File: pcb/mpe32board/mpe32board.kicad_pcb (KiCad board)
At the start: 2 copper layers, 12 parts, among them J1 Conn_ST_STDC14, J3 Conn_01x01_Socket, J4 Conn_01x04, U10 W9812G6KH-75, U2 USBLC6-2P6, U3 AMS1117-3.3, U4 TCA9548ARGER, U5 TCA9548ARGER, U6 TCA9548ARGER, U7 TCA9548ARGER, U8 TCA9548ARGER, U9 STM32H743IITx

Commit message: layout stuff
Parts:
- added C1: 4.7μF, Capacitor_SMD:C_0603_1608Metric, F.Cu at (104.7, 146.2)
- added C10: 100nF, Capacitor_SMD:C_0603_1608Metric, F.Cu at (100.4, 115.2)
- added C11: 100nF, Capacitor_SMD:C_0603_1608Metric, F.Cu at (94.8, 115.1)
- added C12: 100nF, Capacitor_SMD:C_0603_1608Metric, F.Cu at (87.8, 121.0)
- added C13: 100nF, Capacitor_SMD:C_0603_1608Metric, F.Cu at (118.6, 130.5)
- added C14: 100nF, Capacitor_SMD:C_0603_1608Metric, F.Cu at (87.7, 131.8)
- added C15: 2.2μF, Capacitor_SMD:C_0603_1608Metric, F.Cu at (96.3, 115.1)
- added C16: 2.2μF, Capacitor_SMD:C_0603_1608Metric, F.Cu at (87.6, 137.9)
- added C17: 10μF, Capacitor_SMD:C_0603_1608Metric, F.Cu at (125.8, 101.3)
- added C18: 0.1μF, Capacitor_SMD:C_0603_1608Metric, F.Cu at (125.8, 102.9)
- added C19: 10μF, Capacitor_SMD:C_0603_1608Metric, F.Cu at (125.8, 104.5)
- added C2: 100nF, Capacitor_SMD:C_0603_1608Metric, F.Cu at (105.8, 115.2)
- added C20: 0.1μF, Capacitor_SMD:C_0603_1608Metric, F.Cu at (125.8, 106.1)
- added C21: 1μF, Capacitor_SMD:C_0603_1608Metric, F.Cu at (87.7, 133.3)
- added C22: 100nF, Capacitor_SMD:C_0603_1608Metric, F.Cu at (118.6, 134.5)
- added C23: 100nF, Capacitor_SMD:C_0603_1608Metric, F.Cu at (118.6, 139.1)
- added C24: 100nF, Capacitor_SMD:C_0603_1608Metric, F.Cu at (112.0, 146.2)
- added C25: 100nF, Capacitor_SMD:C_0603_1608Metric, F.Cu at (118.5, 122.4)
- added C26: 10μF, Capacitor_SMD:C_0603_1608Metric, F.Cu at (125.4, 112.4)
- added C27: 0.1μF, Capacitor_SMD:C_0603_1608Metric, F.Cu at (126.9, 112.4)
- added C28: 1μF, Capacitor_SMD:C_0603_1608Metric, F.Cu at (123.9, 112.4)
- added C29: 0.1μF, Capacitor_SMD:C_0603_1608Metric, F.Cu at (123.1, 116.1)
- added C3: 100nF, Capacitor_SMD:C_0603_1608Metric, F.Cu at (111.9, 115.3)
- added C30: 10μF, Capacitor_SMD:C_0603_1608Metric, F.Cu at (123.1, 114.6)
- added C31: 0.1μF, Capacitor_SMD:C_0603_1608Metric, F.Cu at (123.1, 117.5)
- added C32: 10μF, Capacitor_SMD:C_0603_1608Metric, F.Cu at (123.1, 119.0)
- added C33: 47μF, Capacitor_SMD:C_0603_1608Metric, F.Cu at (129.8, 112.4)
- added C34: 47μF, Capacitor_SMD:C_0603_1608Metric, F.Cu at (128.4, 112.4)
- added C4: 100nF, Capacitor_SMD:C_0603_1608Metric, F.Cu at (87.7, 126.9)
- added C5: 100nF, Capacitor_SMD:C_0603_1608Metric, F.Cu at (87.6, 139.3)
- added C6: 100nF, Capacitor_SMD:C_0603_1608Metric, F.Cu at (93.9, 146.2)
- added C7: 100nF, Capacitor_SMD:C_0603_1608Metric, F.Cu at (100.5, 146.2)
- added C8: 100nF, Capacitor_SMD:C_0603_1608Metric, F.Cu at (106.2, 146.2)
- added C9: 100nF, Capacitor_SMD:C_0603_1608Metric, F.Cu at (118.6, 124.0)
- added D1: WS2812B, LED_SMD:LED_WS2812B_PLCC4_5.0x5.0mm_P3.2mm, F.Cu at (70.0, 172.0)
- added D2: WS2812B, LED_SMD:LED_WS2812B_PLCC4_5.0x5.0mm_P3.2mm, F.Cu at (79.8, 172.0)
- added D3: WS2812B, LED_SMD:LED_WS2812B_PLCC4_5.0x5.0mm_P3.2mm, F.Cu at (89.6, 172.0)
- added D4: WS2812B, LED_SMD:LED_WS2812B_PLCC4_5.0x5.0mm_P3.2mm, F.Cu at (99.5, 172.0)
- added D5: WS2812B, LED_SMD:LED_WS2812B_PLCC4_5.0x5.0mm_P3.2mm, F.Cu at (109.3, 172.0)
- added D6: WS2812B, LED_SMD:LED_WS2812B_PLCC4_5.0x5.0mm_P3.2mm, F.Cu at (119.1, 172.0)
- added D7: WS2812B, LED_SMD:LED_WS2812B_PLCC4_5.0x5.0mm_P3.2mm, F.Cu at (128.9, 172.0)
- added D8: WS2812B, LED_SMD:LED_WS2812B_PLCC4_5.0x5.0mm_P3.2mm, F.Cu at (138.7, 172.0)
- added J10: Conn_01x04, Connector_JST:JST_SH_BM04B-SRSS-TB_1x04-1MP_P1.00mm_Vertical, F.Cu at (150.6, 140.4)
- added J11: Conn_01x04, Connector_JST:JST_SH_BM04B-SRSS-TB_1x04-1MP_P1.00mm_Vertical, F.Cu at (150.6, 145.7)
- added J12: Conn_01x04, Connector_JST:JST_SH_BM04B-SRSS-TB_1x04-1MP_P1.00mm_Vertical, F.Cu at (150.6, 151.0)
- added J13: Conn_01x04, Connector_JST:JST_SH_BM04B-SRSS-TB_1x04-1MP_P1.00mm_Vertical, F.Cu at (150.6, 156.3)
- added J14: Conn_01x04, Connector_JST:JST_SH_BM04B-SRSS-TB_1x04-1MP_P1.00mm_Vertical, F.Cu at (150.6, 161.6)
- added J15: Conn_01x04, Connector_JST:JST_SH_BM04B-SRSS-TB_1x04-1MP_P1.00mm_Vertical, F.Cu at (150.6, 166.8)
- added J16: Conn_01x04, Connector_JST:JST_SH_BM04B-SRSS-TB_1x04-1MP_P1.00mm_Vertical, F.Cu at (159.1, 108.7)
- added J17: Conn_01x04, Connector_JST:JST_SH_BM04B-SRSS-TB_1x04-1MP_P1.00mm_Vertical, F.Cu at (159.1, 114.0)
- added J18: Conn_01x04, Connector_JST:JST_SH_BM04B-SRSS-TB_1x04-1MP_P1.00mm_Vertical, F.Cu at (159.1, 119.2)
- added J19: Conn_01x04, Connector_JST:JST_SH_BM04B-SRSS-TB_1x04-1MP_P1.00mm_Vertical, F.Cu at (159.1, 124.5)
- added J2: USB_C_Receptacle_USB2.0_16P, Connector_USB:USB_C_Receptacle_GCT_USB4105-xx-A_16P_TopMnt_Horizontal, F.Cu at (121.6, 92.1)
- added J20: Conn_01x04, Connector_JST:JST_SH_BM04B-SRSS-TB_1x04-1MP_P1.00mm_Vertical, F.Cu at (159.1, 129.8)
- added J21: Conn_01x04, Connector_JST:JST_SH_BM04B-SRSS-TB_1x04-1MP_P1.00mm_Vertical, F.Cu at (159.1, 135.1)
- added J22: Conn_01x04, Connector_JST:JST_SH_BM04B-SRSS-TB_1x04-1MP_P1.00mm_Vertical, F.Cu at (159.1, 140.4)
- added J23: Conn_01x04, Connector_JST:JST_SH_BM04B-SRSS-TB_1x04-1MP_P1.00mm_Vertical, F.Cu at (159.1, 145.7)
- added J24: Conn_01x04, Connector_JST:JST_SH_BM04B-SRSS-TB_1x04-1MP_P1.00mm_Vertical, F.Cu at (159.1, 151.0)
- added J25: Conn_01x04, Connector_JST:JST_SH_BM04B-SRSS-TB_1x04-1MP_P1.00mm_Vertical, F.Cu at (159.1, 156.3)
- added J26: Conn_01x04, Connector_JST:JST_SH_BM04B-SRSS-TB_1x04-1MP_P1.00mm_Vertical, F.Cu at (159.1, 161.6)
- added J27: Conn_01x04, Connector_JST:JST_SH_BM04B-SRSS-TB_1x04-1MP_P1.00mm_Vertical, F.Cu at (159.1, 166.8)
- added J28: Conn_01x04, Connector_JST:JST_SH_BM04B-SRSS-TB_1x04-1MP_P1.00mm_Vertical, F.Cu at (167.3, 108.7)
- added J29: Conn_01x04, Connector_JST:JST_SH_BM04B-SRSS-TB_1x04-1MP_P1.00mm_Vertical, F.Cu at (167.3, 114.0)
- added J30: Conn_01x04, Connector_JST:JST_SH_BM04B-SRSS-TB_1x04-1MP_P1.00mm_Vertical, F.Cu at (167.3, 119.2)
- added J31: Conn_01x04, Connector_JST:JST_SH_BM04B-SRSS-TB_1x04-1MP_P1.00mm_Vertical, F.Cu at (167.3, 124.5)
- added J32: Conn_01x04, Connector_JST:JST_SH_BM04B-SRSS-TB_1x04-1MP_P1.00mm_Vertical, F.Cu at (167.3, 129.8)
- added J33: Conn_01x04, Connector_JST:JST_SH_BM04B-SRSS-TB_1x04-1MP_P1.00mm_Vertical, F.Cu at (167.3, 135.1)
- added J34: Conn_01x04, Connector_JST:JST_SH_BM04B-SRSS-TB_1x04-1MP_P1.00mm_Vertical, F.Cu at (167.3, 140.4)
- added J35: Conn_01x04, Connector_JST:JST_SH_BM04B-SRSS-TB_1x04-1MP_P1.00mm_Vertical, F.Cu at (167.3, 145.7)
- added J36: Conn_01x04, Connector_JST:JST_SH_BM04B-SRSS-TB_1x04-1MP_P1.00mm_Vertical, F.Cu at (167.3, 151.0)
- added J37: Conn_01x04, Connector_JST:JST_SH_BM04B-SRSS-TB_1x04-1MP_P1.00mm_Vertical, F.Cu at (167.3, 156.3)
- added J38: Conn_01x04, Connector_JST:JST_SH_BM04B-SRSS-TB_1x04-1MP_P1.00mm_Vertical, F.Cu at (167.3, 161.6)
- added J39: Conn_01x04, Connector_JST:JST_SH_BM04B-SRSS-TB_1x04-1MP_P1.00mm_Vertical, F.Cu at (167.3, 166.8)
- added J40: Conn_01x04, Connector_JST:JST_SH_BM04B-SRSS-TB_1x04-1MP_P1.00mm_Vertical, F.Cu at (147.2, 100.0)
- added J41: Conn_01x04, Connector_JST:JST_SH_BM04B-SRSS-TB_1x04-1MP_P1.00mm_Vertical, F.Cu at (152.4, 100.0)
- added J42: Conn_01x04, Connector_JST:JST_SH_BM04B-SRSS-TB_1x04-1MP_P1.00mm_Vertical, F.Cu at (157.6, 100.0)
- added J43: Conn_01x04, Connector_JST:JST_SH_BM04B-SRSS-TB_1x04-1MP_P1.00mm_Vertical, F.Cu at (162.8, 100.0)
- added J44: Micro_SD_Card, Connector_Card:microSD_HC_Molex_47219-2001, F.Cu at (107.2, 97.1)
- added J45: Conn_01x04_Socket, Connector_PinHeader_2.54mm:PinHeader_1x04_P2.54mm_Vertical, F.Cu at (69.1, 130.4)
- added J46: Conn_02x10_Counter_Clockwise, Connector_PinHeader_2.54mm:PinHeader_2x10_P2.54mm_Vertical, F.Cu at (145.3, 94.0)
- added J47: AudioJack3_Ground, Connector_Audio:Jack_3.5mm_CUI_SJ-3524-SMT_Horizontal, F.Cu at (133.1, 95.1)
- added J5: Conn_01x04, Connector_JST:JST_SH_BM04B-SRSS-TB_1x04-1MP_P1.00mm_Vertical, F.Cu at (150.6, 114.0)
- added J6: Conn_01x04, Connector_JST:JST_SH_BM04B-SRSS-TB_1x04-1MP_P1.00mm_Vertical, F.Cu at (150.6, 119.2)
- added J7: Conn_01x04, Connector_JST:JST_SH_BM04B-SRSS-TB_1x04-1MP_P1.00mm_Vertical, F.Cu at (150.6, 124.5)
- added J8: Conn_01x04, Connector_JST:JST_SH_BM04B-SRSS-TB_1x04-1MP_P1.00mm_Vertical, F.Cu at (150.6, 129.8)
- added J9: Conn_01x04, Connector_JST:JST_SH_BM04B-SRSS-TB_1x04-1MP_P1.00mm_Vertical, F.Cu at (150.6, 135.1)
- added R1: 10kΩ, Resistor_SMD:R_0603_1608Metric, F.Cu at (87.7, 96.1)
- added R10: 2.2kΩ, Resistor_SMD:R_0603_1608Metric, F.Cu at (139.2, 119.5)
- added R11: 2.2kΩ, Resistor_SMD:R_0603_1608Metric, F.Cu at (141.4, 115.7)
- added R12: 2.2kΩ, Resistor_SMD:R_0603_1608Metric, F.Cu at (141.4, 117.2)
- added R13: 2.2kΩ, Resistor_SMD:R_0603_1608Metric, F.Cu at (141.4, 112.7)
- added R14: 2.2kΩ, Resistor_SMD:R_0603_1608Metric, F.Cu at (141.4, 114.2)
- added R15: 2.2kΩ, Resistor_SMD:R_0603_1608Metric, F.Cu at (139.2, 110.5)
- added R16: 2.2kΩ, Resistor_SMD:R_0603_1608Metric, F.Cu at (140.7, 110.5)
- added R17: 2.2kΩ, Resistor_SMD:R_0603_1608Metric, F.Cu at (136.2, 110.5)
- added R18: 2.2kΩ, Resistor_SMD:R_0603_1608Metric, F.Cu at (137.7, 110.5)
- added R19: 2.2kΩ, Resistor_SMD:R_0603_1608Metric, F.Cu at (133.3, 110.5)
- added R2: 10kΩ, Resistor_SMD:R_0603_1608Metric, F.Cu at (87.7, 98.6)
- added R20: 2.2kΩ, Resistor_SMD:R_0603_1608Metric, F.Cu at (134.7, 110.5)
- added R21: 10kΩ, Resistor_SMD:R_0603_1608Metric, F.Cu at (107.6, 146.2)
- added R22: 10kΩ, Resistor_SMD:R_0603_1608Metric, F.Cu at (109.1, 146.2)
- added R23: 10kΩ, Resistor_SMD:R_0603_1608Metric, F.Cu at (114.9, 115.3)
- added R24: 10kΩ, Resistor_SMD:R_0603_1608Metric, F.Cu at (113.4, 115.3)
- added R25: 2.2kΩ, Resistor_SMD:R_0603_1608Metric, F.Cu at (123.7, 147.9)
- added R26: 2.2kΩ, Resistor_SMD:R_0603_1608Metric, F.Cu at (122.2, 147.9)
- added R27: 2.2kΩ, Resistor_SMD:R_0603_1608Metric, F.Cu at (126.7, 147.9)
- added R28: 2.2kΩ, Resistor_SMD:R_0603_1608Metric, F.Cu at (125.2, 147.9)
- added R29: 2.2kΩ, Resistor_SMD:R_0603_1608Metric, F.Cu at (129.6, 147.9)
- added R3: 5.1kΩ, Resistor_SMD:R_0603_1608Metric, F.Cu at (123.7, 97.6)
- added R30: 2.2kΩ, Resistor_SMD:R_0603_1608Metric, F.Cu at (128.2, 147.9)
- added R31: 2.2kΩ, Resistor_SMD:R_0603_1608Metric, F.Cu at (130.3, 144.2)
- added R32: 2.2kΩ, Resistor_SMD:R_0603_1608Metric, F.Cu at (130.3, 145.7)
- added R33: 2.2kΩ, Resistor_SMD:R_0603_1608Metric, F.Cu at (130.3, 141.2)
- added R34: 2.2kΩ, Resistor_SMD:R_0603_1608Metric, F.Cu at (130.3, 142.7)
- added R35: 2.2kΩ, Resistor_SMD:R_0603_1608Metric, F.Cu at (128.1, 139.0)
- added R36: 2.2kΩ, Resistor_SMD:R_0603_1608Metric, F.Cu at (129.6, 139.0)
- added R37: 2.2kΩ, Resistor_SMD:R_0603_1608Metric, F.Cu at (125.2, 139.0)
- added R38: 2.2kΩ, Resistor_SMD:R_0603_1608Metric, F.Cu at (126.7, 139.0)
- added R39: 2.2kΩ, Resistor_SMD:R_0603_1608Metric, F.Cu at (122.3, 139.0)
- added R4: 5.1kΩ, Resistor_SMD:R_0603_1608Metric, F.Cu at (119.4, 98.4)
- added R40: 2.2kΩ, Resistor_SMD:R_0603_1608Metric, F.Cu at (123.7, 139.0)
- added R41: 1kΩ, Resistor_SMD:R_0603_1608Metric, F.Cu at (92.4, 115.1)
- added R42: 1kΩ, Resistor_SMD:R_0603_1608Metric, F.Cu at (87.8, 119.5)
- added R43: 2.2kΩ, Resistor_SMD:R_0603_1608Metric, F.Cu at (123.7, 135.3)
- added R44: 2.2kΩ, Resistor_SMD:R_0603_1608Metric, F.Cu at (122.2, 135.3)
- added R45: 2.2kΩ, Resistor_SMD:R_0603_1608Metric, F.Cu at (126.7, 135.3)
- added R46: 2.2kΩ, Resistor_SMD:R_0603_1608Metric, F.Cu at (125.2, 135.3)
- added R47: 2.2kΩ, Resistor_SMD:R_0603_1608Metric, F.Cu at (129.6, 135.3)
- added R48: 2.2kΩ, Resistor_SMD:R_0603_1608Metric, F.Cu at (128.1, 135.3)
- added R49: 2.2kΩ, Resistor_SMD:R_0603_1608Metric, F.Cu at (130.3, 131.6)
- added R5: 2.2kΩ, Resistor_SMD:R_0603_1608Metric, F.Cu at (134.7, 119.5)
- added R50: 2.2kΩ, Resistor_SMD:R_0603_1608Metric, F.Cu at (130.3, 133.1)
- added R51: 2.2kΩ, Resistor_SMD:R_0603_1608Metric, F.Cu at (130.3, 128.6)
- added R52: 2.2kΩ, Resistor_SMD:R_0603_1608Metric, F.Cu at (130.3, 130.1)
- added R53: 2.2kΩ, Resistor_SMD:R_0603_1608Metric, F.Cu at (128.1, 126.4)
- added R54: 2.2kΩ, Resistor_SMD:R_0603_1608Metric, F.Cu at (129.6, 126.4)
- added R55: 2.2kΩ, Resistor_SMD:R_0603_1608Metric, F.Cu at (125.1, 126.4)
- added R56: 2.2kΩ, Resistor_SMD:R_0603_1608Metric, F.Cu at (126.6, 126.4)
- added R57: 2.2kΩ, Resistor_SMD:R_0603_1608Metric, F.Cu at (122.2, 126.4)
- added R58: 2.2kΩ, Resistor_SMD:R_0603_1608Metric, F.Cu at (123.7, 126.4)
- added R59: 10kΩ, Resistor_SMD:R_0603_1608Metric, F.Cu at (78.8, 150.7)
- added R6: 2.2kΩ, Resistor_SMD:R_0603_1608Metric, F.Cu at (133.2, 119.5)
- added R60: 10kΩ, Resistor_SMD:R_0603_1608Metric, F.Cu at (98.0, 150.7)
- added R61: 2.2kΩ, Resistor_SMD:R_0603_1608Metric, F.Cu at (134.9, 132.9)
- added R62: 2.2kΩ, Resistor_SMD:R_0603_1608Metric, F.Cu at (133.4, 132.9)
- added R63: 2.2kΩ, Resistor_SMD:R_0603_1608Metric, F.Cu at (137.8, 132.9)
- added R64: 2.2kΩ, Resistor_SMD:R_0603_1608Metric, F.Cu at (136.3, 132.9)
- added R65: 2.2kΩ, Resistor_SMD:R_0603_1608Metric, F.Cu at (140.8, 132.9)
- added R66: 2.2kΩ, Resistor_SMD:R_0603_1608Metric, F.Cu at (139.3, 132.9)
- added R67: 2.2kΩ, Resistor_SMD:R_0603_1608Metric, F.Cu at (141.5, 129.2)
- added R68: 2.2kΩ, Resistor_SMD:R_0603_1608Metric, F.Cu at (141.5, 130.6)
- added R69: 2.2kΩ, Resistor_SMD:R_0603_1608Metric, F.Cu at (141.5, 126.2)
- added R7: 2.2kΩ, Resistor_SMD:R_0603_1608Metric, F.Cu at (137.7, 119.5)
- added R70: 2.2kΩ, Resistor_SMD:R_0603_1608Metric, F.Cu at (141.5, 127.7)
- added R71: 2.2kΩ, Resistor_SMD:R_0603_1608Metric, F.Cu at (139.3, 123.9)
- added R72: 2.2kΩ, Resistor_SMD:R_0603_1608Metric, F.Cu at (140.8, 123.9)
- added R73: 2.2kΩ, Resistor_SMD:R_0603_1608Metric, F.Cu at (136.3, 123.9)
- added R74: 2.2kΩ, Resistor_SMD:R_0603_1608Metric, F.Cu at (137.8, 123.9)
- added R75: 2.2kΩ, Resistor_SMD:R_0603_1608Metric, F.Cu at (133.3, 123.9)
- added R76: 2.2kΩ, Resistor_SMD:R_0603_1608Metric, F.Cu at (134.8, 123.9)
- added R77: 10kΩ, Resistor_SMD:R_0603_1608Metric, F.Cu at (117.1, 150.7)
- added R78: 10kΩ, Resistor_SMD:R_0603_1608Metric, F.Cu at (136.2, 150.7)
- added R79: 2.2kΩ, Resistor_SMD:R_0603_1608Metric, F.Cu at (134.9, 147.3)
- added R8: 2.2kΩ, Resistor_SMD:R_0603_1608Metric, F.Cu at (136.2, 119.5)
- added R80: 2.2kΩ, Resistor_SMD:R_0603_1608Metric, F.Cu at (133.4, 147.3)
- added R81: 2.2kΩ, Resistor_SMD:R_0603_1608Metric, F.Cu at (137.8, 147.3)
- added R82: 2.2kΩ, Resistor_SMD:R_0603_1608Metric, F.Cu at (136.4, 147.3)
- added R83: 2.2kΩ, Resistor_SMD:R_0603_1608Metric, F.Cu at (140.8, 147.3)
- added R84: 2.2kΩ, Resistor_SMD:R_0603_1608Metric, F.Cu at (139.3, 147.3)
- added R85: 2.2kΩ, Resistor_SMD:R_0603_1608Metric, F.Cu at (141.5, 143.6)
- added R86: 2.2kΩ, Resistor_SMD:R_0603_1608Metric, F.Cu at (141.5, 145.1)
- added R87: 2.2kΩ, Resistor_SMD:R_0603_1608Metric, F.Cu at (141.5, 140.7)
- added R88: 2.2kΩ, Resistor_SMD:R_0603_1608Metric, F.Cu at (141.5, 142.2)
- added R89: 2.2kΩ, Resistor_SMD:R_0603_1608Metric, F.Cu at (139.3, 138.4)
- added R9: 2.2kΩ, Resistor_SMD:R_0603_1608Metric, F.Cu at (140.7, 119.5)
- added R90: 2.2kΩ, Resistor_SMD:R_0603_1608Metric, F.Cu at (140.8, 138.4)
- added R91: 2.2kΩ, Resistor_SMD:R_0603_1608Metric, F.Cu at (136.3, 138.4)
- added R92: 2.2kΩ, Resistor_SMD:R_0603_1608Metric, F.Cu at (137.8, 138.4)
- added R93: 2.2kΩ, Resistor_SMD:R_0603_1608Metric, F.Cu at (133.4, 138.4)
- added R94: 2.2kΩ, Resistor_SMD:R_0603_1608Metric, F.Cu at (134.9, 138.4)
- added R95: 47kΩ, Resistor_SMD:R_0603_1608Metric, F.Cu at (104.3, 107.4)
- added R96: 47kΩ, Resistor_SMD:R_0603_1608Metric, F.Cu at (101.4, 107.3)
- added R97: 47kΩ, Resistor_SMD:R_0603_1608Metric, F.Cu at (102.8, 107.3)
- added R98: 47kΩ, Resistor_SMD:R_0603_1608Metric, F.Cu at (108.6, 107.3)
- added R99: 47kΩ, Resistor_SMD:R_0603_1608Metric, F.Cu at (110.1, 107.3)
- added SW1: SW_Push, Button_Switch_THT:SW_PUSH_6mm, F.Cu at (91.2, 90.6)
- added SW2: SW_Push, Button_Switch_THT:SW_PUSH_6mm, F.Cu at (91.2, 99.1)
- added SW3: SW_Push, Button_Switch_Keyboard:SW_Cherry_MX_1.00u_PCB, F.Cu at (78.0, 154.0)
- added SW4: SW_Push, Button_Switch_Keyboard:SW_Cherry_MX_1.00u_PCB, F.Cu at (97.1, 154.0)
- added SW5: SW_Push, Button_Switch_Keyboard:SW_Cherry_MX_1.00u_PCB, F.Cu at (116.2, 154.0)
- added SW6: SW_Push, Button_Switch_Keyboard:SW_Cherry_MX_1.00u_PCB, F.Cu at (135.3, 154.0)
- added U1: TAC5212IRGER, 1_udu_lib:VQFN24_RGE_CORNERPADS_TEX-L, F.Cu at (127.3, 116.6)
- moved U5 79.9 mm to (125.5, 143.5), turned to 90 degrees
- moved U6 65.4 mm to (125.5, 130.9), turned to 90 degrees
- moved U9 58.9 mm to (103.2, 130.8), turned to 180 degrees
- moved U8 57.5 mm to (136.7, 142.9), turned to 90 degrees
- moved U10 57.0 mm to (78.4, 130.4), turned to 180 degrees
- moved U4 55.5 mm to (136.6, 115.0), turned to 90 degrees
- moved J1 54.0 mm to (75.3, 97.7), turned to 90 degrees
- moved U7 51.2 mm to (136.7, 128.4), turned to 90 degrees
- moved J3 45.8 mm to (168.0, 98.0)
- moved U3 38.3 mm to (119.6, 105.3), turned to 180 degrees
- moved J4 22.7 mm to (150.6, 108.7)
- moved U2 14.3 mm to (122.0, 100.1)
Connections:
- net SWO renamed JTDO
- U4 pad 19: SCL_0 -> I2C2_SCL
- U4 pad 20: SDA_0 -> I2C2_SDA
- U5 pad 19: SCL_1 -> I2C2_SCL
- U5 pad 20: SDA_1 -> I2C2_SDA
- U5 pad 22: GND -> +3V3
- U6 pad 19: SCL_2 -> I2C2_SCL
- U6 pad 20: SDA_2 -> I2C2_SDA
- U6 pad 23: GND -> +3V3
- U7 pad 19: SCL_3 -> I2C2_SCL
- U7 pad 20: SDA_3 -> I2C2_SDA
- U7 pad 22: GND -> +3V3
- U7 pad 23: GND -> +3V3
- U8 pad 19: SCL_1 -> I2C2_SCL
- U8 pad 20: SDA_1 -> I2C2_SDA
- U9 pad 117: unconnected-(U9-PC8-Pad117) -> SDMMC1_D0
- U9 pad 118: SDA_3 -> SDMMC1_D1
- U9 pad 119: SCL_3 -> unconnected-(U9-PA8-Pad119)
- U9 pad 139: unconnected-(U9-PC10-Pad139) -> SDMMC1_D2
- U9 pad 140: unconnected-(U9-PC11-Pad140) -> SDMMC1_D3
- U9 pad 141: unconnected-(U9-PC12-Pad141) -> SDMMC1_CK
- U9 pad 144: unconnected-(U9-PD2-Pad144) -> SDMMC1_CMD
- U9 pad 164: SCL_0 -> I2C1_SCL
- U9 pad 165: SDA_0 -> I2C1_SDA
- U9 pad 167: SCL_1 -> unconnected-(U9-PB8-Pad167)
- U9 pad 168: SDA_1 -> unconnected-(U9-PB9-Pad168)
- U9 pad 42: unconnected-(U9-PA2-Pad42) -> NEOPIXEL_INTERNAL
- U9 pad 45: unconnected-(U9-PH4-Pad45) -> I2C2_SCL
- U9 pad 46: unconnected-(U9-PH5-Pad46) -> I2C2_SDA
- U9 pad 47: unconnected-(U9-PA3-Pad47) -> NEOPIXEL_IN
- U9 pad 50: unconnected-(U9-PA4-Pad50) -> I2S1_WS
- U9 pad 51: unconnected-(U9-PA5-Pad51) -> I2S1_CK
- U9 pad 52: unconnected-(U9-PA6-Pad52) -> I2S1_SDI
- U9 pad 53: unconnected-(U9-PA7-Pad53) -> I2S1_SDO
- U9 pad 79: SCL_2 -> TAC5212_GPIO1
- U9 pad 80: SDA_2 -> TAC5212_GPIO2
- U9 pad 88: unconnected-(U9-PH11-Pad88) -> I2C4_SCL
- U9 pad 89: unconnected-(U9-PH12-Pad89) -> I2C4_SDA
- U9 pad 92: unconnected-(U9-PB12-Pad92) -> TAC5212_GPO1
- U9 pad 93: unconnected-(U9-PB13-Pad93) -> TAC5212_GPI1
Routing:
- added copper zone on In2.Cu, net +3V3
- added copper zone on In1.Cu, net GND
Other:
- board outline added: 107 x 87 mm
- copper layers 2 -> 4

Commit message: board layout stuff
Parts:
- removed J28, J29, J30, J31, J32, J33, J34, J35, J36, J37, J38, J39, J40, J41, J42, J43: Conn_01x04, Connector_JST:JST_SH_BM04B-SRSS-TB_1x04-1MP_P1.00mm_Vertical
- removed R61, R62, R63, R64, R65, R66, R67, R68, R69, R70, R71, R72, R73, R74, R75, R76, R79, R80, R81, R82, R83, R84, R85, R86, R87, R88, R89, R90, R91, R92, R93, R94: 2.2kΩ, Resistor_SMD:R_0603_1608Metric
- removed U7, U8: TCA9548ARGER, Package_DFN_QFN:Texas_RGE0024C_VQFN-24-1EP_4x4mm_P0.5mm_EP2.1x2.1mm
- added H1: MountingHole_Pad, MountingHole:MountingHole_3.2mm_M3_DIN965_Pad, F.Cu at (72.7, 91.5)
- added H2: MountingHole_Pad, MountingHole:MountingHole_3.2mm_M3_DIN965_Pad, F.Cu at (131.9, 91.5)
- added H3: MountingHole_Pad, MountingHole:MountingHole_3.2mm_M3_DIN965_Pad, F.Cu at (131.9, 135.1)
- added H4: MountingHole_Pad, MountingHole:MountingHole_3.2mm_M3_DIN965_Pad, F.Cu at (72.7, 135.1)
- added J48: Micro_SD_Card_Det_Hirose_DM3AT, Connector_Card:microSD_HC_Hirose_DM3D-SF, F.Cu at (92.3, 87.2)
- added U11: IP4252CZ16, Package_SON:Nexperia_HUSON-16_USON-16-1EP_1.35x3.3mm_P0.4mm_EP0.4x2.8mm, F.Cu at (100.8, 85.0)
- J44: value Micro_SD_Card -> Conn_01x05; footprint Connector_Card:microSD_HC_Molex_47219-2001 -> Connector_Molex:Molex_SL_171971-0005_1x05_P2.54mm_Vertical
- moved J47 67.3 mm to (66.4, 86.0)
- moved C34 58.4 mm to (71.5, 99.6)
- moved C26 58.2 mm to (68.4, 100.4)
- moved C27 58.2 mm to (69.9, 100.4)
- moved C28 58.2 mm to (66.9, 100.4)
- moved C33 58.1 mm to (73.0, 100.4)
- moved C29 58.1 mm to (66.3, 104.1)
- moved C30 58.1 mm to (66.2, 102.6)
- moved C31 58.1 mm to (66.3, 105.6)
- moved C32 58.1 mm to (66.3, 107.1)
- moved U1 57.6 mm to (70.9, 104.7)
- moved J1 49.0 mm to (123.3, 88.1), turned to -90 degrees
- moved J2 44.3 mm to (78.3, 82.8)
- moved R3 43.9 mm to (80.8, 88.3)
- moved R4 43.8 mm to (76.6, 89.1)
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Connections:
- J44 pad 1: SDMMC1_D2 -> +3V3
- J44 pad 2: SDMMC1_D3 -> I2C2_SCL
- J44 pad 3: SDMMC1_CMD -> I2C2_SDA
- J44 pad 4: +3V3 -> RESET_0
- J44 pad 5: SDMMC1_CK -> GND
- U9 pad 134: unconnected-(U9-PI3-Pad134) -> BTN4_INTERNAL
- U9 pad 173: unconnected-(U9-PI4-Pad173) -> BTN3_INTERNAL
- U9 pad 174: unconnected-(U9-PI5-Pad174) -> BTN2_INTERNAL
- U9 pad 175: unconnected-(U9-PI6-Pad175) -> BTN1_INTERNAL
- U9 pad 41: unconnected-(U9-PA1-Pad41) -> SDCARD_DET
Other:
- board size 107 x 87 mm -> 98 x 85 mm

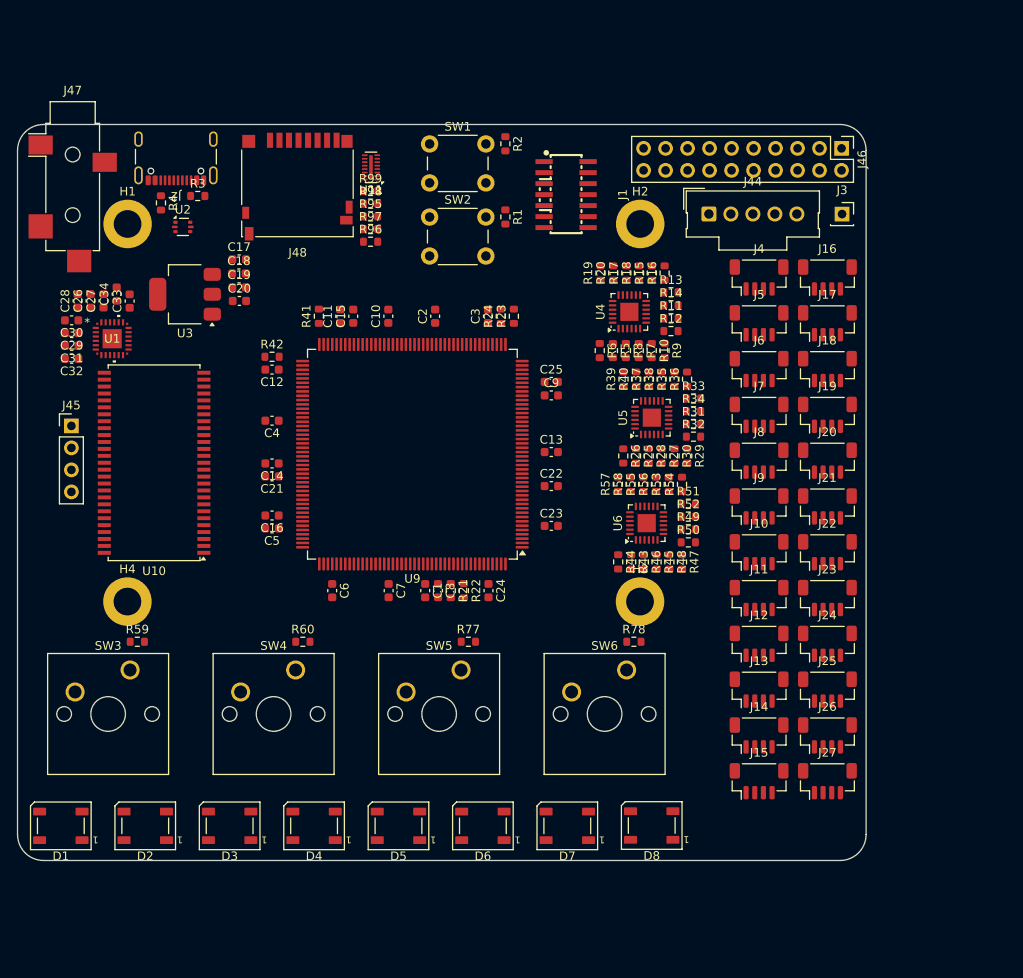
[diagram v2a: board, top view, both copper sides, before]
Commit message: create lcd footprint
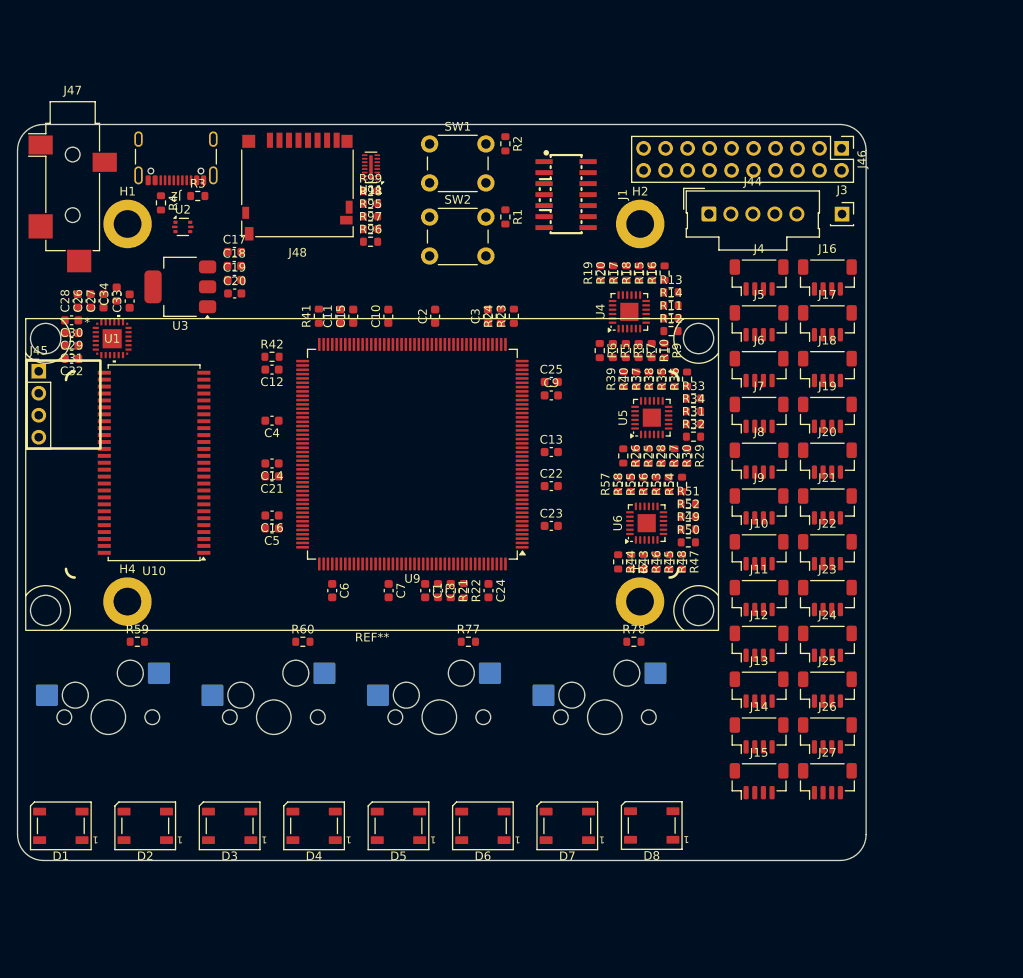
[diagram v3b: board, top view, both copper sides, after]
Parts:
- added REF**: CN0295D, 1_udu_lib:CN0295D, F.Cu at (101.0, 120.4)
- SW3, SW4, SW5, SW6: footprint Button_Switch_Keyboard:SW_Cherry_MX_1.00u_PCB -> mxfoot:MX-Hotswap-1U; moved to B.Cu
- moved J45 7.35 mm to (62.5, 108.5)
- moved SW5 6.00 mm to (108.7, 148.4), turned to 180 degrees
- moved SW3 6.00 mm to (70.5, 148.4), turned to 180 degrees
- moved SW4 6.00 mm to (89.6, 148.4), turned to 180 degrees
- moved SW6 6.00 mm to (127.8, 148.4), turned to 180 degrees
- moved C19 1.02 mm to (85.0, 98.0)
- moved C20 1.02 mm to (85.1, 99.5)
- moved U3 1.02 mm to (78.8, 98.8)
- moved C17 1.02 mm to (85.1, 94.7)
- moved C18 1.02 mm to (85.0, 96.3)

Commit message: routed data bus of ram
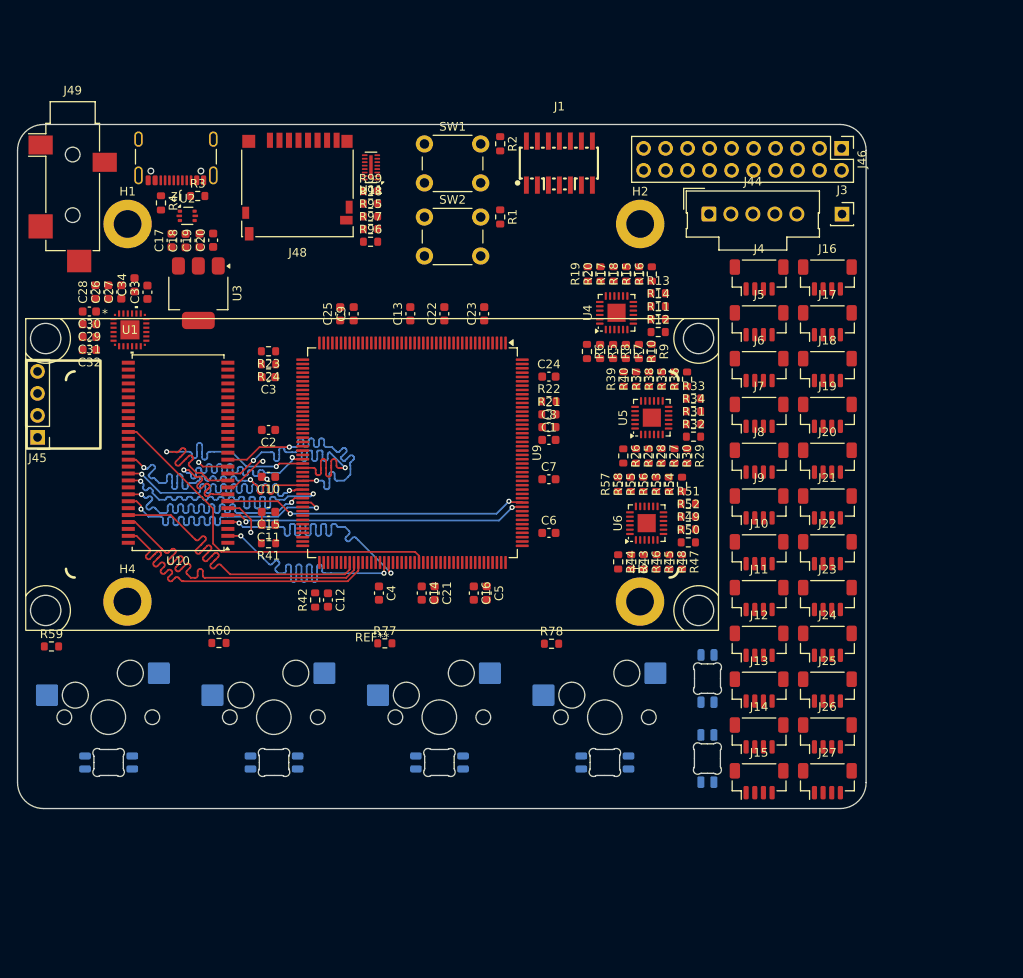
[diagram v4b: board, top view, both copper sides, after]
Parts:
- removed D1, D8: WS2812B, LED_SMD:LED_WS2812B_PLCC4_5.0x5.0mm_P3.2mm
- removed J47: AudioJack3_Ground, Connector_Audio:Jack_3.5mm_CUI_SJ-3524-SMT_Horizontal
- added J49: AudioJack3_SwitchT, Connector_Audio:Jack_3.5mm_CUI_SJ-3524-SMT_Horizontal, F.Cu at (66.4, 86.0)
- D2, D3, D4, D5, D6, D7: value WS2812B -> SK6812MINI-E; footprint LED_SMD:LED_WS2812B_PLCC4_5.0x5.0mm_P3.2mm -> LED_SMD:LED_SK6812MINI-E_3.2x2.8mm_P1.5mm_ReverseMount; moved to B.Cu
- moved D2 67.1 mm to (139.7, 144.0), turned to -90 degrees
- moved D3 55.7 mm to (139.7, 153.2), turned to -90 degrees
- moved D7 53.5 mm to (70.5, 153.7)
- moved D4 34.4 mm to (127.8, 153.7)
- moved R23 28.6 mm to (89.0, 106.2), turned to 180 degrees
- moved R42 28.5 mm to (94.4, 134.9), turned to 90 degrees
- moved R24 27.4 mm to (89.0, 107.7), turned to 180 degrees
- moved C12 27.4 mm to (95.8, 134.9), turned to -90 degrees
- moved R41 26.9 mm to (89.0, 128.4), turned to 180 degrees
- moved C3 26.3 mm to (89.0, 109.2), turned to 180 degrees
- moved C6 25.9 mm to (121.4, 127.2), turned to 0 degrees
- moved C5 25.9 mm to (114.2, 134.1), turned to -90 degrees
- moved C23 25.7 mm to (113.9, 101.9), turned to 90 degrees
- moved C24 25.7 mm to (121.4, 109.1), turned to 0 degrees
- moved C25 25.6 mm to (97.3, 101.9), turned to 90 degrees
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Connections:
- D2 pad 1: +3V3 -> GND
- D2 pad 2: Net-(D2-DOUT) -> NEOPIXEL_INTERNAL
- D2 pad 3: GND -> +3V3
- D2 pad 4: Net-(D1-DOUT) -> Net-(D2-DOUT)
- D3 pad 1: +3V3 -> GND
- D3 pad 2: Net-(D3-DOUT) -> Net-(D2-DOUT)
- D3 pad 3: GND -> +3V3
- D3 pad 4: Net-(D2-DOUT) -> Net-(D3-DOUT)
- D4 pad 1: +3V3 -> GND
- D4 pad 2: Net-(D4-DOUT) -> Net-(D3-DOUT)
- D4 pad 3: GND -> +3V3
- D4 pad 4: Net-(D3-DOUT) -> Net-(D4-DOUT)
- D5 pad 1: +3V3 -> GND
- D5 pad 2: Net-(D5-DOUT) -> Net-(D4-DOUT)
- D5 pad 3: GND -> +3V3
- D5 pad 4: Net-(D4-DOUT) -> Net-(D5-DOUT)
- D6 pad 1: +3V3 -> GND
- D6 pad 2: Net-(D6-DOUT) -> Net-(D5-DOUT)
- D6 pad 3: GND -> +3V3
- D6 pad 4: Net-(D5-DOUT) -> Net-(D6-DOUT)
- D7 pad 1: +3V3 -> GND
- D7 pad 2: Net-(D7-DOUT) -> Net-(D6-DOUT)
- D7 pad 3: GND -> +3V3
- D7 pad 4: Net-(D6-DOUT) -> unconnected-(D7-DOUT-Pad4)
- U9 pad 1: unconnected-(U9-PE2-Pad1) -> NEOPIXEL_INTERNAL
- U9 pad 134: BTN4_INTERNAL -> unconnected-(U9-PI3-Pad134)
- U9 pad 145: unconnected-(U9-PD3-Pad145) -> BTN1_INTERNAL
- U9 pad 146: unconnected-(U9-PD4-Pad146) -> BTN2_INTERNAL
- U9 pad 147: unconnected-(U9-PD5-Pad147) -> BTN3_INTERNAL
- U9 pad 150: unconnected-(U9-PD6-Pad150) -> BTN4_INTERNAL
- U9 pad 173: BTN3_INTERNAL -> unconnected-(U9-PI4-Pad173)
- U9 pad 174: BTN2_INTERNAL -> unconnected-(U9-PI5-Pad174)
- U9 pad 175: BTN1_INTERNAL -> unconnected-(U9-PI6-Pad175)
- U9 pad 42: NEOPIXEL_INTERNAL -> unconnected-(U9-PA2-Pad42)
- U9 pad 44: unconnected-(U9-PH3-Pad44) -> NEOPIXEL_IN
- U9 pad 47: NEOPIXEL_IN -> unconnected-(U9-PA3-Pad47)
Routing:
- net FMC_SDCLK: track 0.00 -> 42.7 mm
- net FMC_D13: track 0.00 -> 38.7 mm
- net FMC_D14: track 0.00 -> 38.6 mm
- net FMC_D15: track 0.00 -> 37.6 mm
- net FMC_D1: track 0.00 -> 35.5 mm, vias 0 -> 2
- net FMC_D6: track 0.00 -> 35.3 mm, vias 0 -> 2
- net FMC_D3: track 0.00 -> 35.2 mm, vias 0 -> 2
- net FMC_D2: track 0.00 -> 35.1 mm, vias 0 -> 2
- net FMC_D0: track 0.00 -> 34.8 mm, vias 0 -> 2
- net FMC_D8: track 0.00 -> 34.7 mm, vias 0 -> 2
- net FMC_D11: track 0.00 -> 34.6 mm, vias 0 -> 2
- net FMC_D10: track 0.00 -> 34.5 mm, vias 0 -> 2
- net FMC_D5: track 0.00 -> 34.5 mm, vias 0 -> 2
- net FMC_D12: track 0.00 -> 34.3 mm, vias 0 -> 2
- net FMC_D9: track 0.00 -> 34.2 mm, vias 0 -> 2
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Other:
- board size 98 x 85 mm -> 98 x 79 mm

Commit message: routed ram
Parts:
- moved R21 35.6 mm to (89.0, 128.3), turned to 180 degrees
- moved R22 34.7 mm to (94.6, 134.1), turned to -90 degrees
- moved C21 34.3 mm to (96.4, 101.9), turned to 90 degrees
- moved R23 33.2 mm to (121.4, 113.4), turned to 0 degrees
- moved R24 32.6 mm to (121.4, 111.9), turned to 0 degrees
- moved R42 26.5 mm to (89.0, 108.9), turned to 180 degrees
- moved R41 20.9 mm to (89.0, 107.5)
- moved C32 9.30 mm to (76.5, 101.6), turned to 0 degrees
- moved C31 8.30 mm to (76.5, 103.1), turned to 0 degrees
- moved C33 7.43 mm to (67.6, 98.3), turned to 180 degrees
- moved C34 6.86 mm to (66.8, 99.8), turned to 180 degrees
- moved C28 5.19 mm to (67.6, 104.4), turned to 180 degrees
- moved U2 5.15 mm to (76.5, 94.7)
- moved C27 4.81 mm to (67.6, 101.4), turned to 180 degrees
- moved C26 4.54 mm to (67.6, 102.9), turned to 180 degrees
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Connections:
- J44 pad 2: I2C2_SCL -> I2C1_SCL
- J44 pad 3: I2C2_SDA -> I2C1_SDA
- J45 pad 1: I2C1_SCL -> I2C4_SCL
- J45 pad 2: I2C1_SDA -> I2C4_SDA
- R21 pad 1: I2C1_SCL -> I2C4_SCL
- R22 pad 1: I2C1_SDA -> I2C4_SDA
- R23 pad 1: I2C2_SCL -> I2C1_SCL
- R24 pad 1: I2C2_SDA -> I2C1_SDA
- R41 pad 1: I2C4_SCL -> I2C2_SCL
- R42 pad 1: I2C4_SDA -> I2C2_SDA
- U1 pad 7: I2C4_SCL -> I2C2_SCL
- U1 pad 8: I2C4_SDA -> I2C2_SDA
- U4 pad 19: I2C2_SCL -> I2C1_SCL
- U4 pad 20: I2C2_SDA -> I2C1_SDA
- U5 pad 19: I2C2_SCL -> I2C1_SCL
- U5 pad 20: I2C2_SDA -> I2C1_SDA
- U6 pad 19: I2C2_SCL -> I2C1_SCL
- U6 pad 20: I2C2_SDA -> I2C1_SDA
- U9 pad 40: unconnected-(U9-PA0-Pad40) -> TAC5212_GPI1
- U9 pad 42: unconnected-(U9-PA2-Pad42) -> TAC5212_GPO1
- U9 pad 92: TAC5212_GPO1 -> unconnected-(U9-PB12-Pad92)
- U9 pad 93: TAC5212_GPI1 -> unconnected-(U9-PB13-Pad93)
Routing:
- net +3V3: track 5.30 -> 67.8 mm, vias 1 -> 6
- net FMC_BA1: track 0.00 -> 59.7 mm, vias 0 -> 4
- net FMC_BA0: track 0.00 -> 59.6 mm, vias 0 -> 4
- net FMC_NBL1: track 0.00 -> 59.0 mm, vias 0 -> 4
- net FMC_SDNCAS: track 0.00 -> 38.2 mm, vias 0 -> 2
- net FMC_NBL0: track 0.00 -> 38.1 mm, vias 0 -> 2
- net FMC_A4: track 0.00 -> 36.4 mm, vias 0 -> 2
- net FMC_A5: track 0.00 -> 35.9 mm, vias 0 -> 2
- net FMC_A9: track 0.00 -> 35.6 mm, vias 0 -> 2
- net FMC_A3: track 0.00 -> 35.5 mm, vias 0 -> 2
- net FMC_A0: track 0.00 -> 35.3 mm, vias 0 -> 2
- net FMC_A11: track 0.00 -> 35.2 mm, vias 0 -> 2
- net FMC_A1: track 0.00 -> 35.0 mm, vias 0 -> 2
- net FMC_A7: track 0.00 -> 34.9 mm, vias 0 -> 2
- net FMC_SDCKE0: track 0.00 -> 34.8 mm, vias 0 -> 2
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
